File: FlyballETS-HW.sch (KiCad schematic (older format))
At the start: 61 parts, among them J1 CONN_01X03, J10 CONN_01X03, J11 CONN_01X03, J12 CONN_01X03, J13 CONN_01X03, J14 CONN_01X03, J15 CONN_01X03, J16 CONN_01X03, J17 CONN_01X03, J18 CONN_01X03, J19 CONN_01X03, J2 CONN_01X03, J20 CONN_01X03, J21 CONN_01X02, J22 CONN_01X02, J23 CONN_01X02, J24 CONN_01X03, J25 CONN_02X09, J26 CONN_01X08, J27 CONN_01X02, J28 Conn_01x04, J3 CONN_01X03, J4 CONN_01X03, J5 CONN_01X03, J6 CONN_01X03, J7 CONN_01X03, J8 CONN_01X03, J9 CONN_01X03, Q1 BC557, Q2 BC557, U1 Wemos_LoLin32, U2 DC-DCStepdown-LM2596

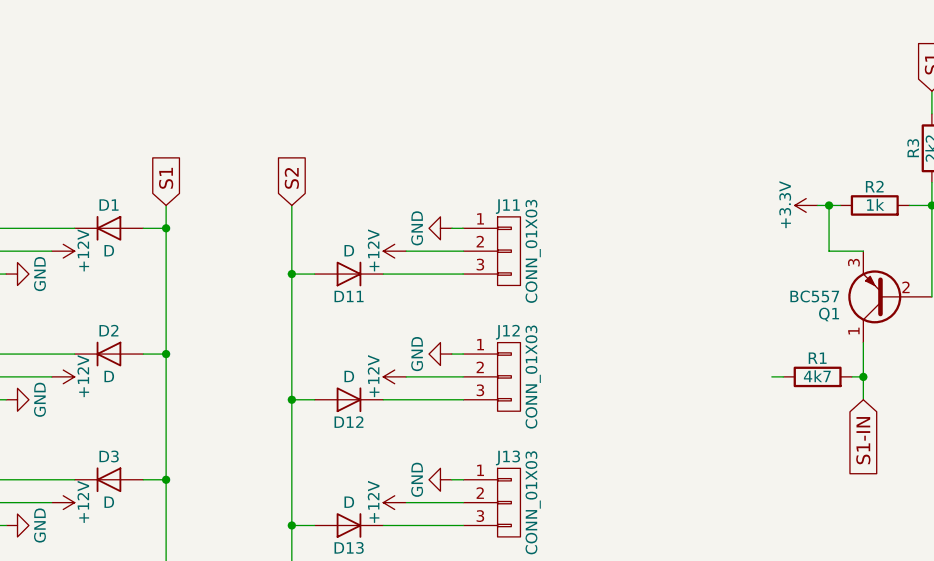
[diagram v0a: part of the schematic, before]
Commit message: Fixed some prototype problems
- Ran final DRC to fix copper planes (fixes #9)
- R1 pad 1 was connected to GND (fixes #10)
- Changed Q1 and Q2 to TO-92 inline wide footprint (fixes #11)
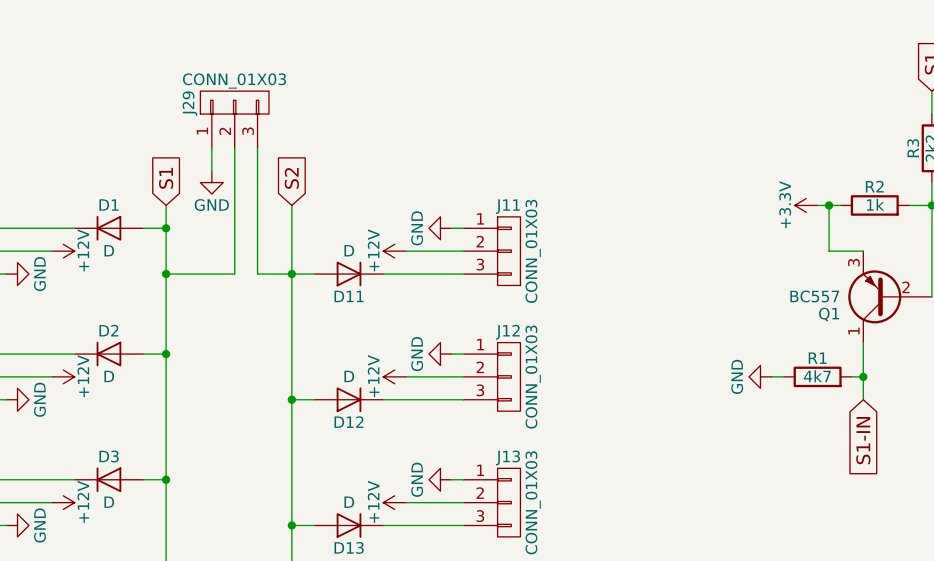
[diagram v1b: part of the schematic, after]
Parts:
- added J29: CONN_01X03, Connectors_JST:JST_XH_B03B-XH-A_03x2.50mm_Straight, symbol CONN_01X03
- Q1, Q2: footprint TO_SOT_Packages_THT:TO-92_Molded_Narrow -> TO_SOT_Packages_THT:TO-92_Inline_Wide
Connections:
- net GND: now also R1.1, J29.1 (P1)
- net S1: now also J29.2 (P2)
- net S2: now also J29.3 (P3)
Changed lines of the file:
@@
 LIBS:contrib
 LIBS:valves
+LIBS:wemos
 LIBS:MyStuff
 LIBS:FlyballETS-HW-cache
@@
 F 0 "Q1" H 5300 2075 50  0000 L CNN
 F 1 "BC557" H 5300 2000 50  0000 L CNN
-F 2 "TO_SOT_Packages_THT:TO-92_Molded_Narrow" H 5300 1925 50  0001 L CIN
+F 2 "TO_SOT_Packages_THT:TO-92_Inline_Wide" H 5300 1925 50  0001 L CIN
 F 3 "" H 5100 2000 50  0001 L CNN
 	1    5100 2000
@@
 F 0 "Q2" H 5950 2075 50  0000 L CNN
 F 1 "BC557" H 5950 2000 50  0000 L CNN
-F 2 "TO_SOT_Packages_THT:TO-92_Molded_Narrow" H 5950 1925 50  0001 L CIN
+F 2 "TO_SOT_Packages_THT:TO-92_Inline_Wide" H 5950 1925 50  0001 L CIN
 F 3 "" H 5750 2000 50  0001 L CNN
 	1    5750 2000
@@
 	3250 1900 2900 1900
 Wire Wire Line
-	2500 1900 2600 1900
+	2350 1900 2600 1900
 Connection ~ 2500 6850
 Connection ~ 2500 6300
@@
 	7750 4550 8400 4550
 $Comp
-L +3.3V #PWR?
+L +3.3V #PWR074
 U 1 1 59AB669C
 P 10200 3850
-F 0 "#PWR?" H 10200 3700 50  0001 C CNN
+F 0 "#PWR074" H 10200 3700 50  0001 C CNN
 F 1 "+3.3V" H 10200 3990 50  0000 C CNN
 F 2 "" H 10200 3850 50  0001 C CNN
@@
 	0    1    1    0
 $EndComp
+$Comp
+L GND #PWR075
+U 1 1 59C0EB5B
+P 4600 2350
+F 0 "#PWR075" H 4600 2100 50  0001 C CNN
+F 1 "GND" H 4600 2200 50  0000 C CNN
+F 2 "" H 4600 2350 50  0001 C CNN
+F 3 "" H 4600 2350 50  0001 C CNN
+	1    4600 2350
+	0    1    -1   0
+$EndComp
+$Comp
+L CONN_01X03 J29
+U 1 1 59C2EC8C
+P 2250 1150
+F 0 "J29" H 2250 1350 50  0000 C CNN
+F 1 "CONN_01X03" V 2350 1150 50  0000 C CNN
+F 2 "Connectors_JST:JST_XH_B03B-XH-A_03x2.50mm_Straight" H 2250 1150 50  0001 C CNN
+F 3 "" H 2250 1150 50  0001 C CNN
+	1    2250 1150
+	0    -1   -1   0
+$EndComp
+$Comp
+L GND #PWR076
+U 1 1 59C2EDCA
+P 2150 1450
+F 0 "#PWR076" H 2150 1200 50  0001 C CNN
+F 1 "GND" H 2150 1300 50  0000 C CNN
+F 2 "" H 2150 1450 50  0001 C CNN
+F 3 "" H 2150 1450 50  0001 C CNN
+	1    2150 1450
+	1    0    0    -1
+$EndComp
+Wire Wire Line
+	2150 1350 2150 1450
+Wire Wire Line
+	2250 1350 2250 1900
+Wire Wire Line
+	2250 1900 1950 1900
+Connection ~ 1950 1900
+Wire Wire Line
+	2350 1350 2350 1900
 $EndSCHEMATC

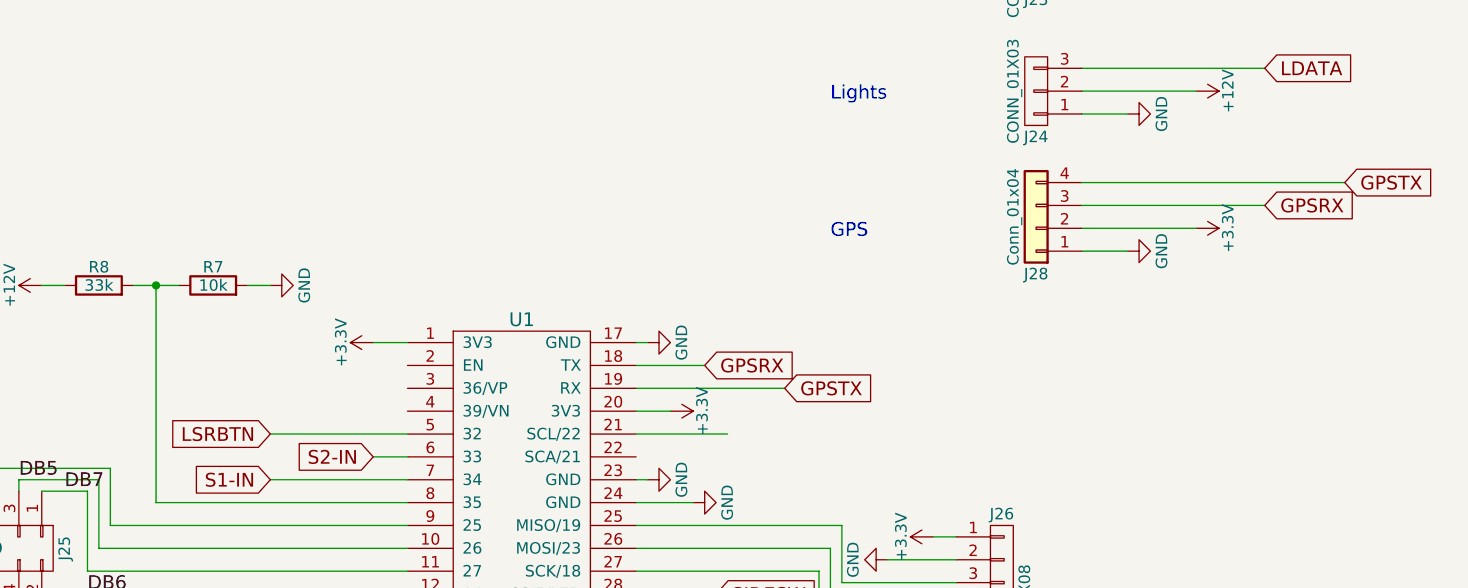
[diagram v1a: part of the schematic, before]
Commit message: Corrected GPS connections
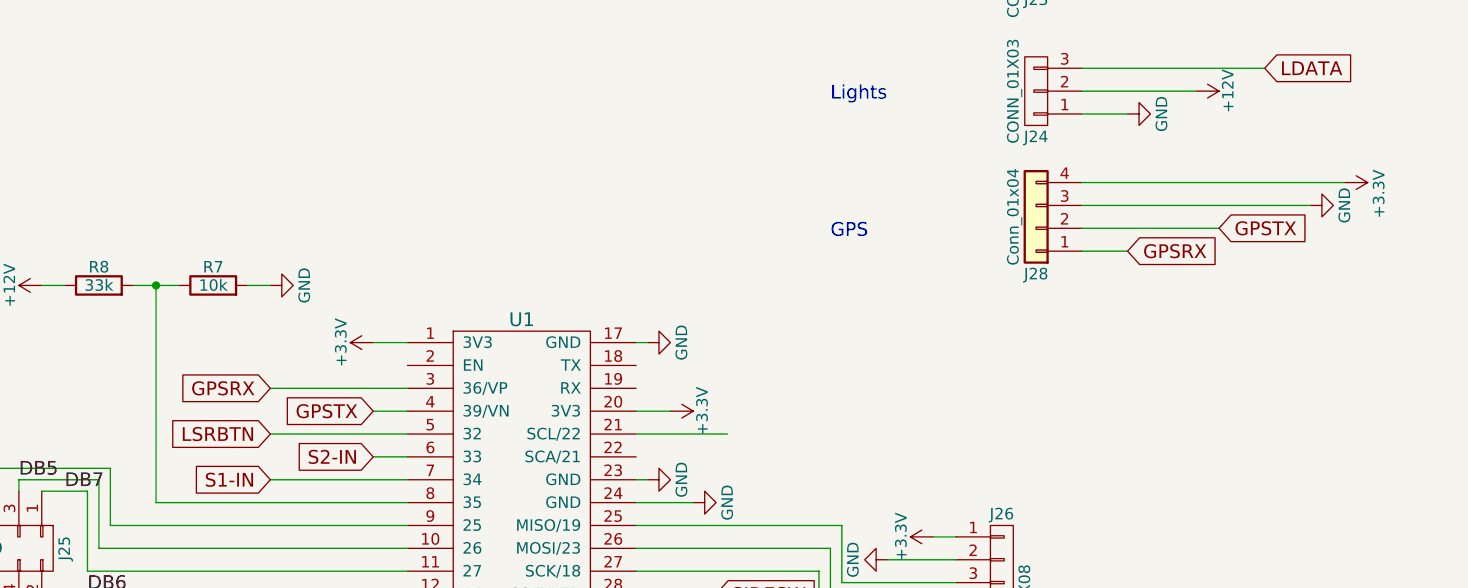
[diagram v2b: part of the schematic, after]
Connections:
- net +3V3: now also J28.4 (Pin_4); no longer J28.2 (Pin_2)
- net GND: now also J28.3 (Pin_3); no longer J28.1 (Pin_1)
- net GPSRX: now also J28.1 (Pin_1), U1.3 (36/VP); no longer J28.3 (Pin_3), U1.18 (TX)
- net GPSTX: now also J28.2 (Pin_2), U1.4 (39/VN); no longer J28.4 (Pin_4), U1.19 (RX)
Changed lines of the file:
@@
 LIBS:contrib
 LIBS:valves
-LIBS:wemos
 LIBS:MyStuff
 LIBS:FlyballETS-HW-cache
@@
 L GND #PWR073
 U 1 1 59AB3DCC
-P 9900 3950
-F 0 "#PWR073" H 9900 3700 50  0001 C CNN
-F 1 "GND" H 9900 3800 50  0000 C CNN
-F 2 "" H 9900 3950 50  0001 C CNN
-F 3 "" H 9900 3950 50  0001 C CNN
-	1    9900 3950
-	0    -1   -1   0
-$EndComp
-Text GLabel 10500 3750 2    60   Input ~ 0
+P 10700 3750
+F 0 "#PWR073" H 10700 3500 50  0001 C CNN
+F 1 "GND" H 10700 3600 50  0000 C CNN
+F 2 "" H 10700 3750 50  0001 C CNN
+F 3 "" H 10700 3750 50  0001 C CNN
+	1    10700 3750
+	0    -1   -1   0
+$EndComp
+Text GLabel 9900 3950 2    60   Input ~ 0
 GPSRX
 Wire Wire Line
-	9700 3750 10500 3750
-Wire Wire Line
-	9700 3850 10200 3850
+	9700 3750 10700 3750
+Wire Wire Line
+	9700 3850 10300 3850
 Wire Wire Line
 	9700 3950 9900 3950
@@
 	-1   0    0    1
 $EndComp
-Text GLabel 10850 3650 2    60   Input ~ 0
+Text GLabel 10300 3850 2    60   Input ~ 0
 GPSTX
 Wire Wire Line
@@
 Wire Wire Line
 	7750 5450 8100 5450
-Text GLabel 8050 4450 2    60   Input ~ 0
+Text GLabel 6600 4650 0    60   Input ~ 0
+GPSTX
+Text GLabel 6150 4550 0    60   Input ~ 0
 GPSRX
-Text GLabel 8400 4550 2    60   Input ~ 0
-GPSTX
-Wire Wire Line
-	7750 4450 8050 4450
-Wire Wire Line
-	7750 4550 8400 4550
 $Comp
 L +3.3V #PWR074
 U 1 1 59AB669C
-P 10200 3850
-F 0 "#PWR074" H 10200 3700 50  0001 C CNN
-F 1 "+3.3V" H 10200 3990 50  0000 C CNN
-F 2 "" H 10200 3850 50  0001 C CNN
-F 3 "" H 10200 3850 50  0001 C CNN
-	1    10200 3850
+P 10850 3650
+F 0 "#PWR074" H 10850 3500 50  0001 C CNN
+F 1 "+3.3V" H 10900 3800 50  0000 C CNN
+F 2 "" H 10850 3650 50  0001 C CNN
+F 3 "" H 10850 3650 50  0001 C CNN
+	1    10850 3650
 	0    1    1    0
 $EndComp
@@
 Wire Wire Line
 	2350 1350 2350 1900
+Wire Wire Line
+	6600 4650 6750 4650
+Wire Wire Line
+	6150 4550 6750 4550
 $EndSCHEMATC

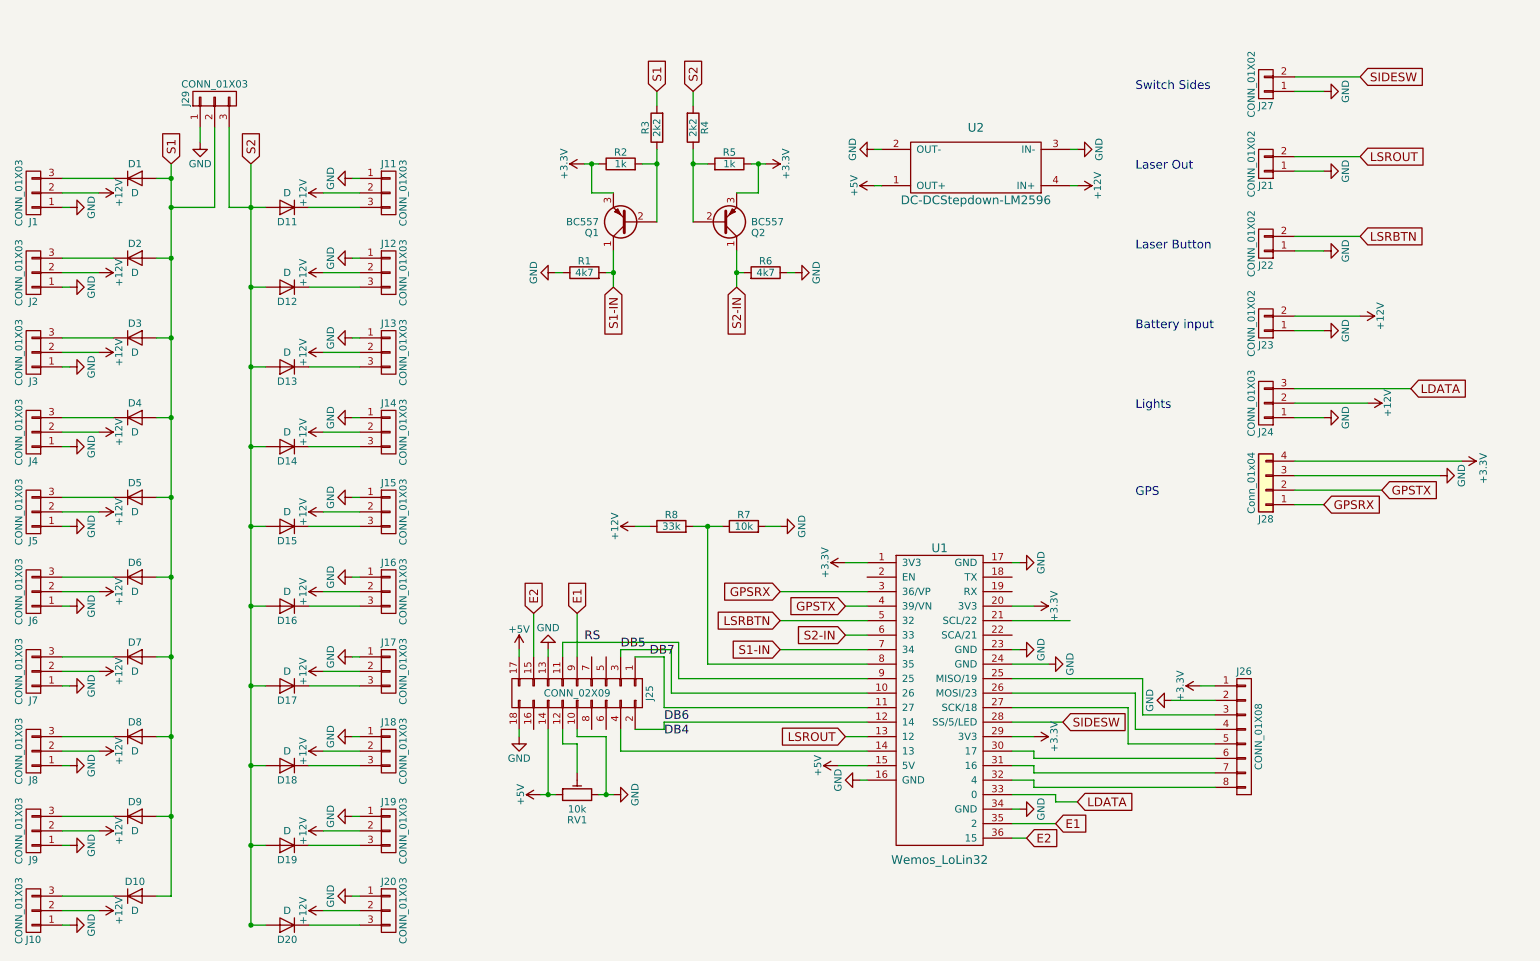
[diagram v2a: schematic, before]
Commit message: Fixed smaller issues
- Added mounting holes
- Added 1000uF cap for Ws2811 lights
- Added 300R resistor in WS2811 data line
- Removed  transistors to invert sensor signal (we need to use NPN, NO from now on)
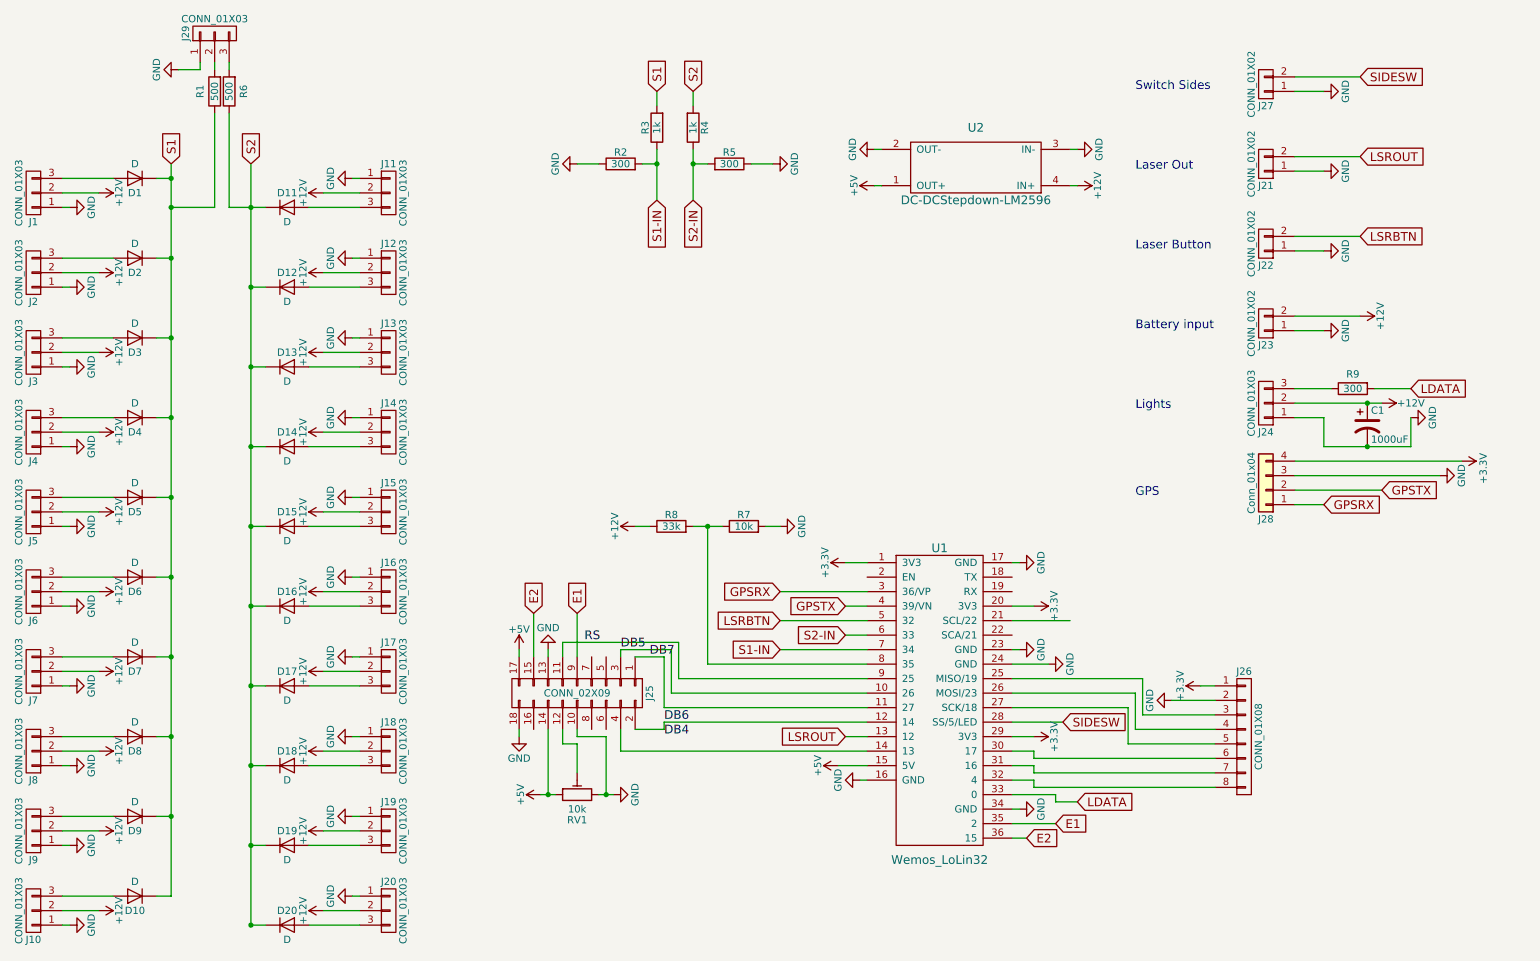
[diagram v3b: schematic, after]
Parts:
- removed Q1, Q2: BC557, TO_SOT_Packages_THT:TO-92_Inline_Wide, symbol BC557
- added C1: 1000uF, Capacitors_THT:CP_Radial_D10.0mm_P5.00mm, symbol CP1
- added R9: 300, Resistors_THT:R_Axial_DIN0207_L6.3mm_D2.5mm_P7.62mm_Horizontal, symbol R
- R1, R6: value 4k7 -> 500
- R2, R5: value 1k -> 300
- R3, R4: value 2k2 -> 1k
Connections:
- net +12V: now also C1.1
- net +3V3: no longer R2.1, R5.1
- net GND: now also R2.1, R5.1, C1.2; no longer R1.1, R6.1
- net LDATA: now also R9.2; no longer J24.3 (P3)
- net S1: now also D1.1 (K), D10.1 (K), D2.1 (K), D3.1 (K), D4.1 (K), D5.1 (K), D6.1 (K), D7.1 (K), D8.1 (K), D9.1 (K), R1.1; no longer D1.2 (A), D10.2 (A), D2.2 (A), D3.2 (A), D4.2 (A), D5.2 (A), D6.2 (A), D7.2 (A), D8.2 (A), D9.2 (A), J29.2 (P2)
- net S1-IN: now also R2.2, R3.1; no longer R1.2
- net S2: now also D11.1 (K), D12.1 (K), D13.1 (K), D14.1 (K), D15.1 (K), D16.1 (K), D17.1 (K), D18.1 (K), D19.1 (K), D20.1 (K), R6.1; no longer D11.2 (A), D12.2 (A), D13.2 (A), D14.2 (A), D15.2 (A), D16.2 (A), D17.2 (A), D18.2 (A), D19.2 (A), D20.2 (A), J29.3 (P3)
- net S2-IN: now also R4.1, R5.2; no longer R6.2
- net at J1.3 (P3): now also D1.2 (A); no longer D1.1 (K)
- net at J2.3 (P3): now also D2.2 (A); no longer D2.1 (K)
- net at J3.3 (P3): now also D3.2 (A); no longer D3.1 (K)
- net at J4.3 (P3): now also D4.2 (A); no longer D4.1 (K)
- net at J5.3 (P3): now also D5.2 (A); no longer D5.1 (K)
- net at J6.3 (P3): now also D6.2 (A); no longer D6.1 (K)
- net at J7.3 (P3): now also D7.2 (A); no longer D7.1 (K)
- net at J8.3 (P3): now also D8.2 (A); no longer D8.1 (K)
- net at J9.3 (P3): now also D9.2 (A); no longer D9.1 (K)
- net at J10.3 (P3): now also D10.2 (A); no longer D10.1 (K)
- net at J20.3 (P3): now also D20.2 (A); no longer D20.1 (K)
- net at J19.3 (P3): now also D19.2 (A); no longer D19.1 (K)
- net at J18.3 (P3): now also D18.2 (A); no longer D18.1 (K)
- net at J17.3 (P3): now also D17.2 (A); no longer D17.1 (K)
- net at J16.3 (P3): now also D16.2 (A); no longer D16.1 (K)
- net at J15.3 (P3): now also D15.2 (A); no longer D15.1 (K)
- net at J14.3 (P3): now also D14.2 (A); no longer D14.1 (K)
- net at J13.3 (P3): now also D13.2 (A); no longer D13.1 (K)
- net at J12.3 (P3): now also D12.2 (A); no longer D12.1 (K)
- net at J11.3 (P3): now also D11.2 (A); no longer D11.1 (K)
- new net: J24.3 (P3), R9.1
- new net: J29.2 (P2), R1.2
- new net: J29.3 (P3), R6.2
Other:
- moved on the sheet: J29

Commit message: Final version
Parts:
- R2, R5: value 300 -> 330
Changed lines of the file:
@@
 P 5800 1600
 F 0 "R5" V 5880 1600 50  0000 C CNN
-F 1 "300" V 5800 1600 50  0000 C CNN
+F 1 "330" V 5800 1600 50  0000 C CNN
 F 2 "Resistors_THT:R_Axial_DIN0207_L6.3mm_D2.5mm_P7.62mm_Horizontal" V 5730 1600 50  0001 C CNN
 F 3 "" H 5800 1600 50  0001 C CNN
@@
 P 5050 1600
 F 0 "R2" V 5130 1600 50  0000 C CNN
-F 1 "300" V 5050 1600 50  0000 C CNN
+F 1 "330" V 5050 1600 50  0000 C CNN
 F 2 "Resistors_THT:R_Axial_DIN0207_L6.3mm_D2.5mm_P7.62mm_Horizontal" V 4980 1600 50  0001 C CNN
 F 3 "" H 5050 1600 50  0001 C CNN
